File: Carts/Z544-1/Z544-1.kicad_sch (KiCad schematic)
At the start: 46 parts, among them IC101 MSM6653A-MCU, IC102 74HC273, IC103 HM9264LF15, IC104 uPD23C16000WGX, IC105 uPD23C8000XGX, IC106 BA15218F, IC107 TC7W139, J1 Loopy-Cart-Edge, X101 4.096MHz

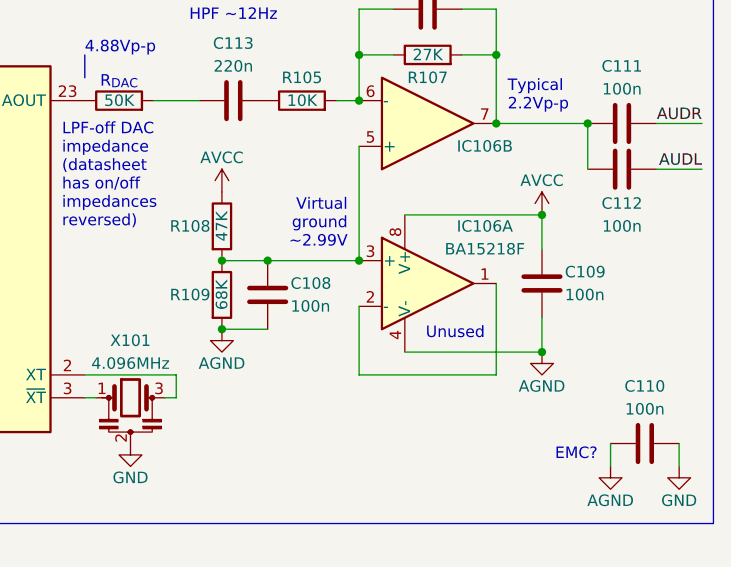
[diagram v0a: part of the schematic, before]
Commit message: Unify project part libs
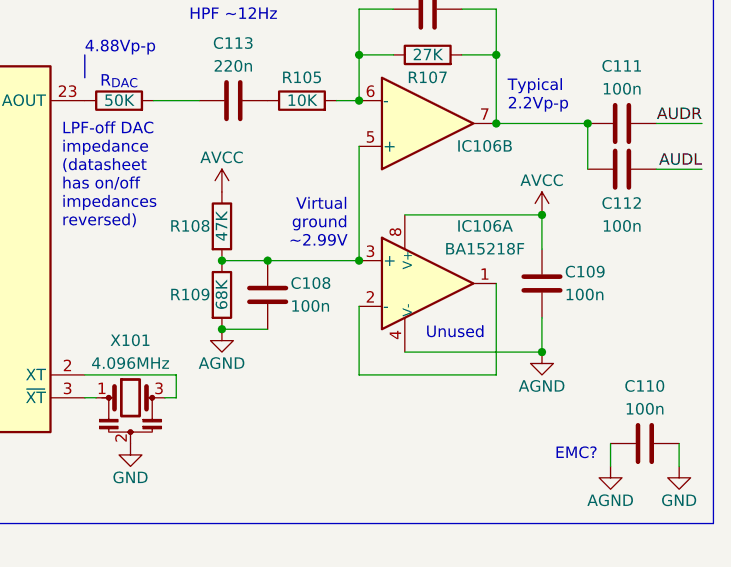
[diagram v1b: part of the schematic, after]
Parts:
- IC101: symbol project-parts:MSM6653A-MCU -> loopy-parts:MSM6653A-MCU
- IC103: symbol project-parts:SRAM_64Kbit_SOP28_Physical -> loopy-parts:SRAM_64Kbit_SOP28_Physical
- IC104: symbol project-parts:ROM_32Mbit_SOP44_Physical -> loopy-parts:ROM_32Mbit_SOP44_Physical
- IC105: symbol project-parts:ROM_8Mbit_SOP44_Physical -> loopy-parts:ROM_8Mbit_SOP44_Physical
- IC106: symbol project-parts:BA15218F -> loopy-parts:BA15218F
- IC107: symbol project-parts:TC7W139F -> loopy-parts:TC7W139F
- J1: footprint project-parts:Loopy-Cart-Edge -> loopy-parts:Loopy_Cart_Edge; symbol project-parts:Loopy-Cart-Edge -> loopy-parts:Loopy_Cart_Edge
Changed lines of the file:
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@@
 	)
 	(symbol
-		(lib_id "project-parts:ROM_32Mbit_SOP44_Physical")
+		(lib_id "loopy-parts:ROM_32Mbit_SOP44_Physical")
 		(at 124.46 49.53 0)
 		(unit 1)
@@
 	)
 	(symbol
-		(lib_id "project-parts:ROM_8Mbit_SOP44_Physical")
+		(lib_id "loopy-parts:ROM_8Mbit_SOP44_Physical")
 		(at 182.88 49.53 0)
 		(unit 1)
@@
 	)
 	(symbol
-		(lib_id "project-parts:BA15218F")
+		(lib_id "loopy-parts:BA15218F")
 		(at 251.46 119.38 0)
 		(mirror x)
@@
 	)
 	(symbol
-		(lib_id "project-parts:SRAM_64Kbit_SOP28_Physical")
+		(lib_id "loopy-parts:SRAM_64Kbit_SOP28_Physical")
 		(at 241.3 39.37 0)
 		(unit 1)
@@
 	)
 	(symbol
-		(lib_id "project-parts:TC7W139F")
+		(lib_id "loopy-parts:TC7W139F")
 		(at 106.68 102.87 0)
 		(unit 1)
@@
 	)
 	(symbol
-		(lib_id "project-parts:MSM6653A-MCU")
+		(lib_id "loopy-parts:MSM6653A-MCU")
 		(at 200.66 133.35 0)
 		(unit 1)
@@
 	)
 	(symbol
-		(lib_id "project-parts:Loopy-Cart-Edge")
+		(lib_id "loopy-parts:Loopy_Cart_Edge")
 		(at 48.26 96.52 0)
 		(unit 1)
@@
 			)
 		)
-		(property "Footprint" "project-parts:Loopy-Cart-Edge"
+		(property "Footprint" "loopy-parts:Loopy_Cart_Edge"
 			(at 48.26 38.1 0)
 			(effects
@@
 	)
 	(symbol
-		(lib_id "project-parts:BA15218F")
+		(lib_id "loopy-parts:BA15218F")
 		(at 251.46 137.16 0)
 		(unit 1)
@@
 	)
 	(symbol
-		(lib_id "project-parts:BA15218F")
+		(lib_id "loopy-parts:BA15218F")
 		(at 251.46 137.16 0)
 		(unit 3)
